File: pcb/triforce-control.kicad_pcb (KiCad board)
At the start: 2 copper layers, 75 x 86 mm, 18 parts, among them CON1 Conn_01x08, CON2 Conn_01x08, CON3 CON_ESC_W1, CON4 CON_ESC_W2, CON5 CON_ESC_W3, CON6 CON_ESC_D1, CON7 CON_ESC_D2, CON8 CON_ESC_D3, CON9 Conn_01x04, U1 ADAFRUIT_HUZZAH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

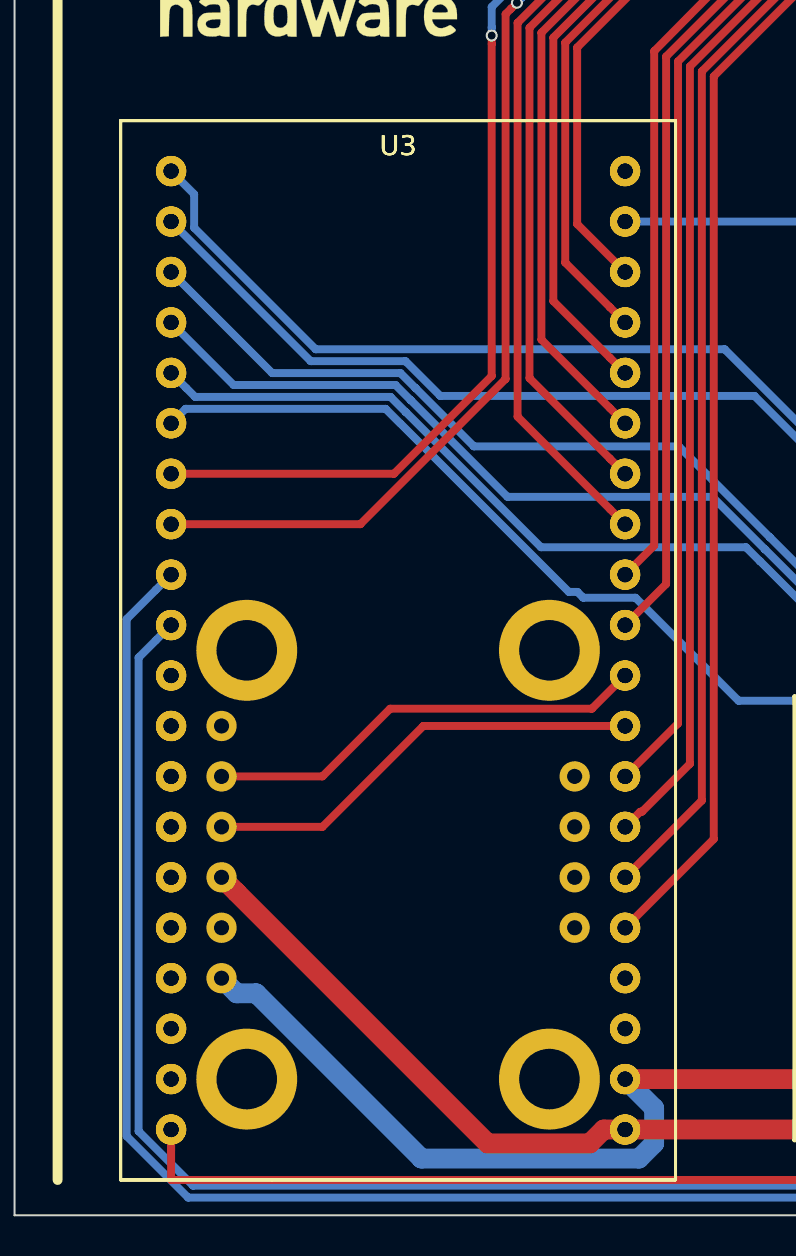
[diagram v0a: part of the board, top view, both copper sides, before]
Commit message: Moved PCB to pcb folder.
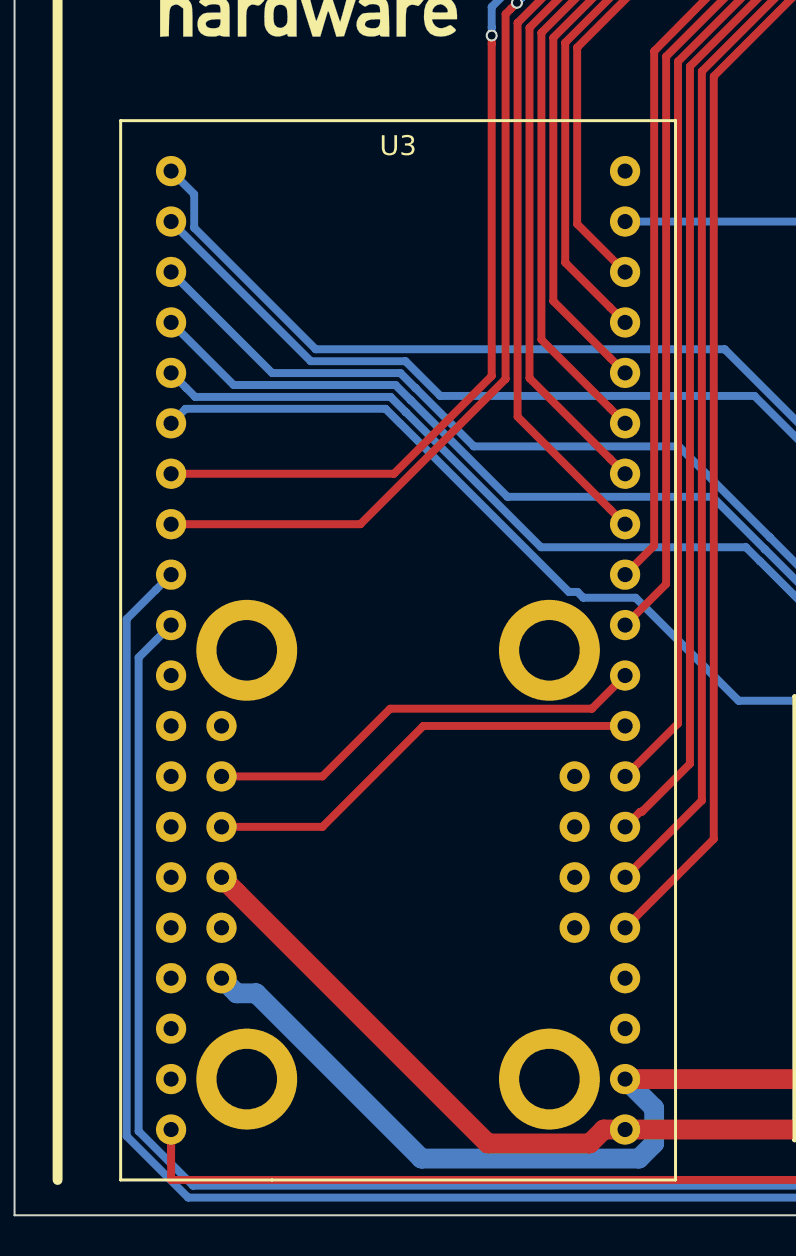
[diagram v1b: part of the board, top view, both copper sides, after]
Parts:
- removed the U3 at (145.4, 84.0)
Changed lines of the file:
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@@
 (kicad_pcb (version 4) (host pcbnew 4.0.7-e2-6376~58~ubuntu16.04.1)
   (general
-    (links 92)
+    (links 52)
     (no_connects 0)
     (area 112.068999 53.108999 187.169001 139.209001)
@@
     (tracks 304)
     (zones 0)
-    (modules 18)
+    (modules 17)
     (nets 71)
   )
@@
     (pad 40 thru_hole circle (at 25.4 -50.8 180) (size 1.524 1.524) (drill 0.762) (layers *.Cu *.Mask)
       (net 66 MBED_3V3))
-    (model Pin_Headers.3dshapes/Pin_Header_Straight_1x20_Pitch2.54mm.wrl
-      (at (xyz 1 2 0.39))
+    (model TriforceFightController.3dshapes/PinHeader_1x20_P2.54mm_Vertical.wrl
+      (at (xyz 1 2 0.35))
       (scale (xyz 1 1 1))
       (rotate (xyz 0 180 0))
     )
-    (model Pin_Headers.3dshapes/Pin_Header_Straight_1x20_Pitch2.54mm.wrl
-      (at (xyz 0.1 2 0.39))
+    (model TriforceFightController.3dshapes/PinHeader_1x20_P2.54mm_Vertical.wrl
+      (at (xyz 0.1 2 0.4))
       (scale (xyz 1 1 1))
       (rotate (xyz 0 180 0))
     )
-    (model /home/cameron/git/triforce-control-pcb/lib/mbed/PinSocket_1x20_P2.54mm_Vertical.wrl
+    (model TriforceFightController.3dshapes/PinSocket_1x20_P2.54mm_Vertical.wrl
       (at (xyz 1 2 0))
       (scale (xyz 1 1 1))
       (rotate (xyz 0 0 0))
     )
-    (model /home/cameron/git/triforce-control-pcb/lib/mbed/PinSocket_1x20_P2.54mm_Vertical.wrl
-      (at (xyz 0.1 2 0))
-      (scale (xyz 1 1 1))
-      (rotate (xyz 0 0 0))
-    )
-  )
-  (module mbed:lpc1768 locked (layer F.Cu)
-    (at 145.401 84.041 180)
-    (fp_text reference U3 (at 13.97 -1.27 180) (layer F.SilkS)
-      (effects (font (size 1 1) (thickness 0.15)))
-    )
-    (fp_text value LPC1768 (at 15.24 -47.49 180) (layer F.Fab)
-      (effects (font (size 1 1) (thickness 0.15)))
-    )
-    (fp_line (start 20.32 -53.34) (end 27.94 -53.34) (layer F.SilkS) (width 0.15))
-    (fp_line (start 27.94 -53.34) (end 27.94 0) (layer F.SilkS) (width 0.15))
-    (fp_line (start 27.94 0) (end 0 0) (layer F.SilkS) (width 0.15))
-    (fp_line (start 0 0) (end 0 -53.34) (layer F.SilkS) (width 0.15))
-    (fp_line (start 0 -53.34) (end 20.32 -53.34) (layer F.SilkS) (width 0.15))
-    (pad 1 thru_hole circle (at 2.54 -50.8 180) (size 1.524 1.524) (drill 0.762) (layers *.Cu *.Mask)
-      (net 1 GND))
-    (pad 2 thru_hole circle (at 2.54 -48.26 180) (size 1.524 1.524) (drill 0.762) (layers *.Cu *.Mask)
-      (net 2 +5V))
-    (pad 3 thru_hole circle (at 2.54 -45.72 180) (size 1.524 1.524) (drill 0.762) (layers *.Cu *.Mask)
-      (net 23 "Net-(U3-Pad3)"))
-    (pad 4 thru_hole circle (at 2.54 -43.18 180) (size 1.524 1.524) (drill 0.762) (layers *.Cu *.Mask)
-      (net 24 "Net-(U3-Pad4)"))
-    (pad 5 thru_hole circle (at 2.54 -40.64 180) (size 1.524 1.524) (drill 0.762) (layers *.Cu *.Mask)
-      (net 57 IN_RX_W6))
-    (pad 6 thru_hole circle (at 2.54 -38.1 180) (size 1.524 1.524) (drill 0.762) (layers *.Cu *.Mask)
-      (net 56 IN_RX_W5))
-    (pad 7 thru_hole circle (at 2.54 -35.56 180) (size 1.524 1.524) (drill 0.762) (layers *.Cu *.Mask)
-      (net 55 IN_RX_W4))
-    (pad 8 thru_hole circle (at 2.54 -33.02 180) (size 1.524 1.524) (drill 0.762) (layers *.Cu *.Mask)
-      (net 54 IN_RX_W3))
-    (pad 9 thru_hole circle (at 2.54 -30.48 180) (size 1.524 1.524) (drill 0.762) (layers *.Cu *.Mask)
-      (net 3 BNO_MBED_SDA))
-    (pad 10 thru_hole circle (at 2.54 -27.94 180) (size 1.524 1.524) (drill 0.762) (layers *.Cu *.Mask)
-      (net 4 BNO_MBED_SCL))
-    (pad 11 thru_hole circle (at 2.54 -25.4 180) (size 1.524 1.524) (drill 0.762) (layers *.Cu *.Mask)
-      (net 53 IN_RX_W2))
-    (pad 12 thru_hole circle (at 2.54 -22.86 180) (size 1.524 1.524) (drill 0.762) (layers *.Cu *.Mask)
-      (net 52 IN_RX_W1))
-    (pad 13 thru_hole circle (at 2.54 -20.32 180) (size 1.524 1.524) (drill 0.762) (layers *.Cu *.Mask)
-      (net 58 IN_RX_D1))
-    (pad 14 thru_hole circle (at 2.54 -17.78 180) (size 1.524 1.524) (drill 0.762) (layers *.Cu *.Mask)
-      (net 59 IN_RX_D2))
-    (pad 15 thru_hole circle (at 2.54 -15.24 180) (size 1.524 1.524) (drill 0.762) (layers *.Cu *.Mask)
-      (net 60 IN_RX_D3))
-    (pad 16 thru_hole circle (at 2.54 -12.7 180) (size 1.524 1.524) (drill 0.762) (layers *.Cu *.Mask)
-      (net 61 IN_RX_D4))
-    (pad 17 thru_hole circle (at 2.54 -10.16 180) (size 1.524 1.524) (drill 0.762) (layers *.Cu *.Mask)
-      (net 62 IN_RX_D5))
-    (pad 18 thru_hole circle (at 2.54 -7.62 180) (size 1.524 1.524) (drill 0.762) (layers *.Cu *.Mask)
-      (net 63 IN_RX_D6))
-    (pad 19 thru_hole circle (at 2.54 -5.08 180) (size 1.524 1.524) (drill 0.762) (layers *.Cu *.Mask)
-      (net 13 ESP_READY))
-    (pad 20 thru_hole circle (at 2.54 -2.54 180) (size 1.524 1.524) (drill 0.762) (layers *.Cu *.Mask)
-      (net 25 "Net-(U3-Pad20)"))
-    (pad 21 thru_hole circle (at 25.4 -2.54 180) (size 1.524 1.524) (drill 0.762) (layers *.Cu *.Mask)
-      (net 7 PWM_OUT_DRV_MOTOR_3))
-    (pad 22 thru_hole circle (at 25.4 -5.08 180) (size 1.524 1.524) (drill 0.762) (layers *.Cu *.Mask)
-      (net 6 PWM_OUT_DRV_MOTOR_2))
-    (pad 23 thru_hole circle (at 25.4 -7.62 180) (size 1.524 1.524) (drill 0.762) (layers *.Cu *.Mask)
-      (net 5 PWM_OUT_DRV_MOTOR_1))
-    (pad 24 thru_hole circle (at 25.4 -10.16 180) (size 1.524 1.524) (drill 0.762) (layers *.Cu *.Mask)
-      (net 10 PWM_OUT_WPN_MOTOR_3))
-    (pad 25 thru_hole circle (at 25.4 -12.7 180) (size 1.524 1.524) (drill 0.762) (layers *.Cu *.Mask)
-      (net 9 PWM_OUT_WPN_MOTOR_2))
-    (pad 26 thru_hole circle (at 25.4 -15.24 180) (size 1.524 1.524) (drill 0.762) (layers *.Cu *.Mask)
-      (net 8 PWM_OUT_WPN_MOTOR_1))
-    (pad 27 thru_hole circle (at 25.4 -17.78 180) (size 1.524 1.524) (drill 0.762) (layers *.Cu *.Mask)
-      (net 11 ESP_MBED_RX))
-    (pad 28 thru_hole circle (at 25.4 -20.32 180) (size 1.524 1.524) (drill 0.762) (layers *.Cu *.Mask)
-      (net 12 ESP_MBED_TX))
-    (pad 30 thru_hole circle (at 25.4 -25.4 180) (size 1.524 1.524) (drill 0.762) (layers *.Cu *.Mask)
-      (net 64 CAN_RXD))
-    (pad 31 thru_hole circle (at 25.4 -27.94 180) (size 1.524 1.524) (drill 0.762) (layers *.Cu *.Mask)
-      (net 26 "Net-(U3-Pad31)"))
-    (pad 32 thru_hole circle (at 25.4 -30.48 180) (size 1.524 1.524) (drill 0.762) (layers *.Cu *.Mask)
-      (net 27 "Net-(U3-Pad32)"))
-    (pad 33 thru_hole circle (at 25.4 -33.02 180) (size 1.524 1.524) (drill 0.762) (layers *.Cu *.Mask)
-      (net 28 "Net-(U3-Pad33)"))
-    (pad 34 thru_hole circle (at 25.4 -35.56 180) (size 1.524 1.524) (drill 0.762) (layers *.Cu *.Mask)
-      (net 29 "Net-(U3-Pad34)"))
-    (pad 35 thru_hole circle (at 25.4 -38.1 180) (size 1.524 1.524) (drill 0.762) (layers *.Cu *.Mask)
-      (net 30 "Net-(U3-Pad35)"))
-    (pad 36 thru_hole circle (at 25.4 -40.64 180) (size 1.524 1.524) (drill 0.762) (layers *.Cu *.Mask)
-      (net 31 "Net-(U3-Pad36)"))
-    (pad 37 thru_hole circle (at 25.4 -43.18 180) (size 1.524 1.524) (drill 0.762) (layers *.Cu *.Mask)
-      (net 32 "Net-(U3-Pad37)"))
-    (pad 38 thru_hole circle (at 25.4 -45.72 180) (size 1.524 1.524) (drill 0.762) (layers *.Cu *.Mask)
-      (net 33 "Net-(U3-Pad38)"))
-    (pad 39 thru_hole circle (at 25.4 -48.26 180) (size 1.524 1.524) (drill 0.762) (layers *.Cu *.Mask)
-      (net 34 "Net-(U3-Pad39)"))
-    (pad 29 thru_hole circle (at 25.4 -22.86 180) (size 1.524 1.524) (drill 0.762) (layers *.Cu *.Mask)
-      (net 65 CAN_TXD))
-    (pad 40 thru_hole circle (at 25.4 -50.8 180) (size 1.524 1.524) (drill 0.762) (layers *.Cu *.Mask)
-      (net 66 MBED_3V3))
-    (model Pin_Headers.3dshapes/Pin_Header_Straight_1x20_Pitch2.54mm.wrl
-      (at (xyz 1 2 0.35))
-      (scale (xyz 1 1 1))
-      (rotate (xyz 0 180 0))
-    )
-    (model Pin_Headers.3dshapes/Pin_Header_Straight_1x20_Pitch2.54mm.wrl
-      (at (xyz 0.1 2 0.4))
-      (scale (xyz 1 1 1))
-      (rotate (xyz 0 180 0))
-    )
-    (model /home/cameron/git/triforce-control-pcb/lib/mbed/PinSocket_1x20_P2.54mm_Vertical.wrl
-      (at (xyz 1 2 0))
-      (scale (xyz 1 1 1))
-      (rotate (xyz 0 0 0))
-    )
-    (model /home/cameron/git/triforce-control-pcb/lib/mbed/PinSocket_1x20_P2.54mm_Vertical.wrl
+    (model TriforceFightController.3dshapes/PinSocket_1x20_P2.54mm_Vertical.wrl
       (at (xyz 0.1 2 0))
       (scale (xyz 1 1 1))
@@
     (pad 4 thru_hole oval (at 6 0) (size 1.2 1.7) (drill 0.75) (layers *.Cu *.Mask)
       (net 2 +5V))
-    (model ${KISYS3DMOD}/Connectors_JST.3dshapes/JST_PH_S4B-PH-K_04x2.00mm_Angled.wrl
+    (model TriforceFightController.3dshapes/JST_PH_S4B-PH-K_04x2.00mm_Angled.wrl
       (at (xyz 0 0 0))
       (scale (xyz 1 1 1))
@@
       (rotate (xyz 0 180 0))
     )
-    (model /home/cameron/git/triforce-control-pcb/lib/mbed/PinSocket_1x10_P2.54mm_Vertical.wrl
+    (model ../library/PinSocket_1x10_P2.54mm_Vertical.wrl
       (at (xyz -0.2 -0.1 0))
       (scale (xyz 1 1 1))
       (rotate (xyz 0 0 0))
     )
-    (model /home/cameron/git/triforce-control-pcb/lib/mbed/PinSocket_1x10_P2.54mm_Vertical.wrl
+    (model ../library/PinSocket_1x10_P2.54mm_Vertical.wrl
       (at (xyz 0.6 -0.1 0))
       (scale (xyz 1 1 1))
@@
     (pad "" smd rect (at -4.8 -1.9375) (size 1.2 1.8) (layers B.Cu B.Paste B.Mask))
     (pad "" smd rect (at 4.8 -1.9375) (size 1.2 1.8) (layers B.Cu B.Paste B.Mask))
-    (model /home/cameron/git/triforce-control-pcb/lib/mbed/SM08B-SRSS.wrl
+    (model TriforceFightController.3dshapes/SM08B-SRSS.wrl
       (at (xyz 0 0.05 -0.02))
       (scale (xyz 1 1 1))
@@
     (pad "" smd rect (at -4.8 -1.9375) (size 1.2 1.8) (layers B.Cu B.Paste B.Mask))
     (pad "" smd rect (at 4.8 -1.9375) (size 1.2 1.8) (layers B.Cu B.Paste B.Mask))
-    (model /home/cameron/git/triforce-control-pcb/lib/mbed/SM08B-SRSS.wrl
+    (model TriforceFightController.3dshapes/SM08B-SRSS.wrl
       (at (xyz 0 0.05 -0.02))
       (scale (xyz 1 1 1))

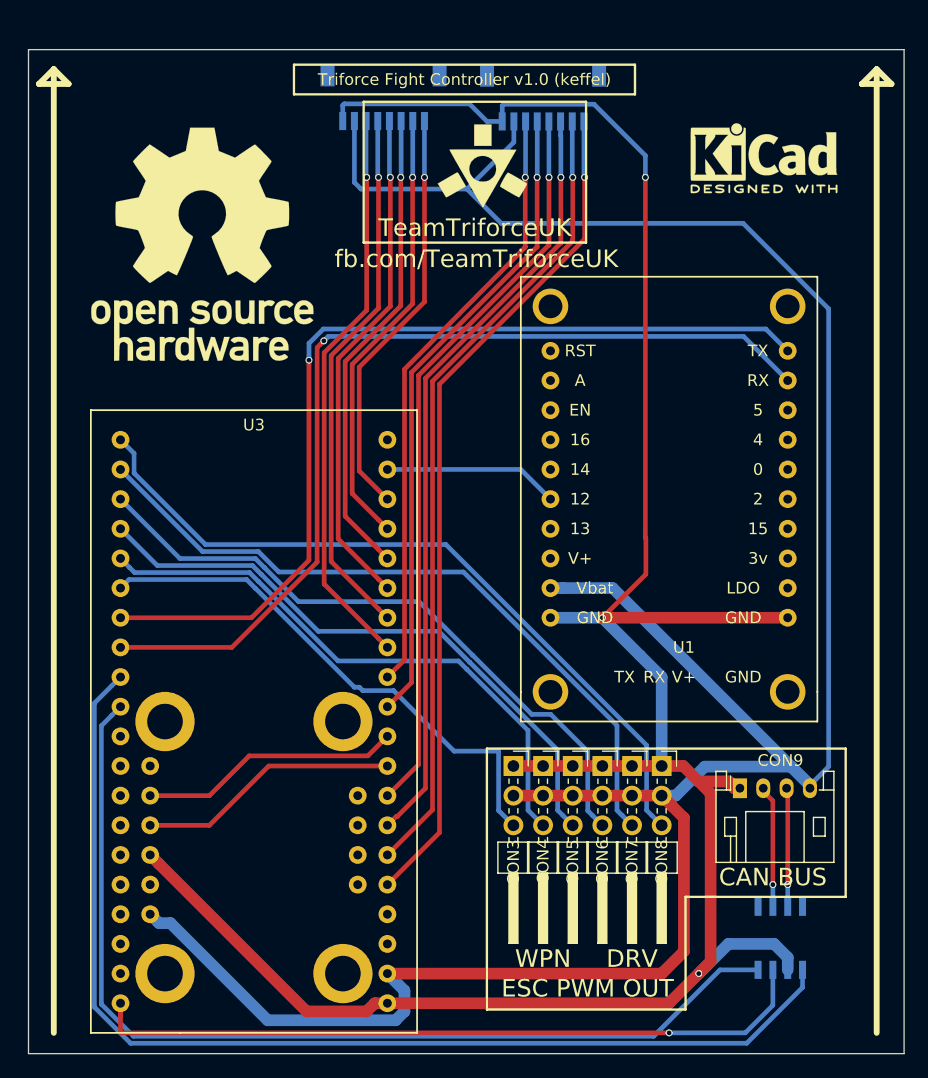
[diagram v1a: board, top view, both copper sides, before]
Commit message: Started moving component source files to external repository.
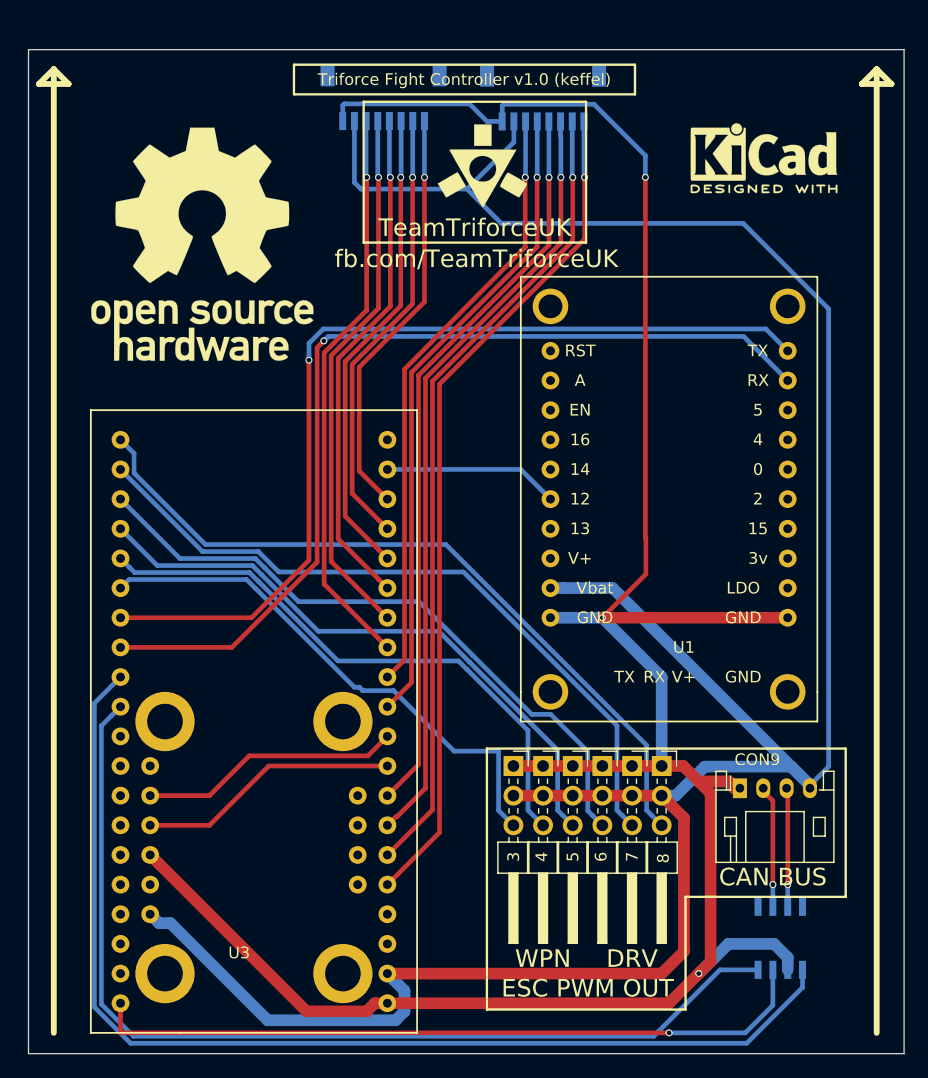
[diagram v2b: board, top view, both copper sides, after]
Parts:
- 3: renamed from CON3; footprint mbed:Pin_Header_Angled_3x01_Pitch2.54mm -> Triforce_Fight_Controller:Pin_Header_Angled_3x01_Pitch2.54mm
- 4: renamed from CON4; footprint mbed:Pin_Header_Angled_3x01_Pitch2.54mm -> Triforce_Fight_Controller:Pin_Header_Angled_3x01_Pitch2.54mm
- 5: renamed from CON5; footprint mbed:Pin_Header_Angled_3x01_Pitch2.54mm -> Triforce_Fight_Controller:Pin_Header_Angled_3x01_Pitch2.54mm
- 6: renamed from CON6; footprint mbed:Pin_Header_Angled_3x01_Pitch2.54mm -> Triforce_Fight_Controller:Pin_Header_Angled_3x01_Pitch2.54mm
- 7: renamed from CON7; footprint mbed:Pin_Header_Angled_3x01_Pitch2.54mm -> Triforce_Fight_Controller:Pin_Header_Angled_3x01_Pitch2.54mm
- 8: renamed from CON8; footprint mbed:Pin_Header_Angled_3x01_Pitch2.54mm -> Triforce_Fight_Controller:Pin_Header_Angled_3x01_Pitch2.54mm
- CON1, CON2: footprint Connectors_JST:JST_SH_SM08B-SRSS-TB_08x1.00mm_Angled -> Triforce_Fight_Controller:JST_SH_SM08B-SRSS-TB_08x1.00mm_Angled
- CON9: footprint Connectors_JST:JST_PH_S4B-PH-K_04x2.00mm_Angled -> Triforce_Fight_Controller:JST_PH_S4B-PH-K_04x2.00mm_Angled
- G***: footprint mbed:logo_small -> Triforce_Fight_Controller:logo_small
- U1: footprint mbed:ESP8266 -> Triforce_Fight_Controller:ESP8266
- U2: footprint mbed:BNO055 -> Triforce_Fight_Controller:BNO055
- U3: footprint mbed:lpc1768 -> Triforce_Fight_Controller:lpc1768
- U4: footprint Housings_SOIC:SOIC-8_3.9x4.9mm_Pitch1.27mm -> Triforce_Fight_Controller:SOIC-8_3.9x4.9mm_Pitch1.27mm
